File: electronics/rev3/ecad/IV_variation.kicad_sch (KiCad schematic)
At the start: 35 parts, among them Q5 TIP122, Q6 TIP127, U2 LMC6484A

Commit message: REV3 schematic
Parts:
- removed HS1, HS2: 15.60°C/W, symbol Mechanical:Heatsink
- removed Q5: TIP122, Package_TO_SOT_THT:TO-220-3_Vertical, symbol Transistor_BJT:TIP122
- removed Q6: TIP127, Package_TO_SOT_THT:TO-220-3_Vertical, symbol Transistor_BJT:TIP127
- removed R6, R7: 10k, Resistor_THT:R_Axial_DIN0207_L6.3mm_D2.5mm_P7.62mm_Horizontal, symbol Device:R_US
- removed R?: 1k, Resistor_THT:R_Axial_DIN0207_L6.3mm_D2.5mm_P7.62mm_Horizontal, symbol Device:R_US
- removed TP6: TestPoint, TestPoint:TestPoint_THTPad_D2.5mm_Drill1.2mm, symbol Connector:TestPoint
- removed unit 1 of U2
- added C10: 0.1uF, Capacitor_THT:C_Disc_D6.0mm_W2.5mm_P5.00mm, symbol Device:C
- added J1: DUT Connector, TerminalBlock_Phoenix:TerminalBlock_Phoenix_MKDS-1,5-2-5.08_1x02_P5.08mm_Horizontal, symbol Connector:Screw_Terminal_01x02
- added R36: 1.5, Resistor_THT:R_Axial_DIN0207_L6.3mm_D2.5mm_P7.62mm_Horizontal, symbol Device:R_US
- C7, C8: footprint (none) -> Capacitor_THT:C_Disc_D6.0mm_W2.5mm_P5.00mm; Distributor Part # (none) -> BC2662CT-ND; Part # (none) -> K103K10X7RF5UH5; Unit Price (none) -> 0.22
- D2: Distributor Part # (none) -> SA13CACT-ND; Part # (none) -> SA13CA; Unit Price (none) -> 0.49
- D3, D4, D5: Distributor Part # (none) -> 1727-2115-1-ND; Part # (none) -> BZX79-C2V4,113; Unit Price (none) -> 0.16
- F?: value 1A -> 1.5A; Distributor Part # (none) -> 507-1893-1-ND; Part # (none) -> 0685T1500-01; Unit Price (none) -> 0.32
- R10, R19: Distributor Part # (none) -> 1712-YR1B11K8CCCT-ND; Part # (none) -> YR1B11K8CC; Unit Price (none) -> 0.63
- R14, R15, R16, R17: Distributor Part # (none) -> A105970CT-ND; Part # (none) -> YR1B10KCC; Unit Price (none) -> 0.63
- R18, R20, R28, R8: Distributor Part # (none) -> A105942CT-ND; Part # (none) -> YR1B1K0CC; Unit Price (none) -> 0.63
- R23, R5: Distributor Part # (none) -> 1712-YR1B3K83CCCT-ND; Part # (none) -> YR1B3K83CC; Unit Price (none) -> 0.63
- R29: value 4.7k -> 3.83k+/-0.1%
- R30: Distributor Part # (none) -> 13-MFR-25FRF52-1KCT-ND; Part # (none) -> MFR-25FRF52-1K; Unit Price (none) -> 0.1
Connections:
- net GND: now also C10.2
- net Vmiddle: now also C10.1
- net V/2: now also R18.1, R29.1, R?.2
- net DUT+: no longer names the net of D2.2 (A2), R16.1, TP1.1
- net DUT+: now also J1.2 (Pin_2), R36.2
- net DUT-: no longer names the net of D2.1 (A1), F?.1, R15.1, TP5.1
- net DUT-: now also J1.1 (Pin_1)
- new net Sweep Voltage Buffer/Sweep_Amplified: R36.1
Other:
- added sheet Sweep Voltage Buffer (sweep_voltage_buffer.kicad_sch)
- sheet Half Supply Buffer ports: added V/2; removed none
- note added: "1.5W"
- note added: "4W"
- moved on the sheet: C7, C8, D2, D3, D4, D5, F?, R10, R14, R15, R16, R17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

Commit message: Layout work
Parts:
- added R?: 1+/-1%, Resistor_SMD:R_2512_6332Metric_Pad1.40x3.35mm_HandSolder, symbol Device:R_US
- F?: value 1.5A -> 1A
- R29: Distributor Part # (none) -> 1712-YR1B3K83CCCT-ND; Part # (none) -> YR1B3K83CC; Unit Price (none) -> 0.63
- R36: footprint Resistor_THT:R_Axial_DIN0207_L6.3mm_D2.5mm_P7.62mm_Horizontal -> Resistor_SMD:R_2512_6332Metric_Pad1.40x3.35mm_HandSolder; Distributor Part # (none) -> A121179CT-ND; Part # (none) -> 35221R5JT; Unit Price (none) -> 1.22
- R?: value 0.5+/-0.1% -> 1+/-1%; footprint Resistor_THT:R_Axial_DIN0207_L6.3mm_D2.5mm_P7.62mm_Horizontal -> Resistor_SMD:R_2512_6332Metric_Pad1.40x3.35mm_HandSolder; Distributor Part # (none) -> RMCF2512FT1R00CT-ND; Part # (none) -> RMCF2512FT1R00; Unit Price (none) -> 0.27
- TP1, TP3, TP4: Distributor Part # (none) -> 36-4952-ND; Part # (none) -> 4952; Unit Price (none) -> 0.26
- TP5: value TestPoint -> 4952; Distributor Part # (none) -> 36-4952-ND; Part # (none) -> 4952; Unit Price (none) -> 0.26
- U2: Distributor Part # (none) -> LMC6484IN/NOPB-ND; Part # (none) -> LMC6484IN/NOPB; Unit Price (none) -> 2.83
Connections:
- net V/2: now also R?.2
- net at F?.2, R8.1, R?.1: now also R?.1
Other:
- note added: "1W"
- note removed: "1.5W"
- moved on the sheet: C10, C7, C8, D2, D3, D4, D5, F?, J1, R10, R14, R15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

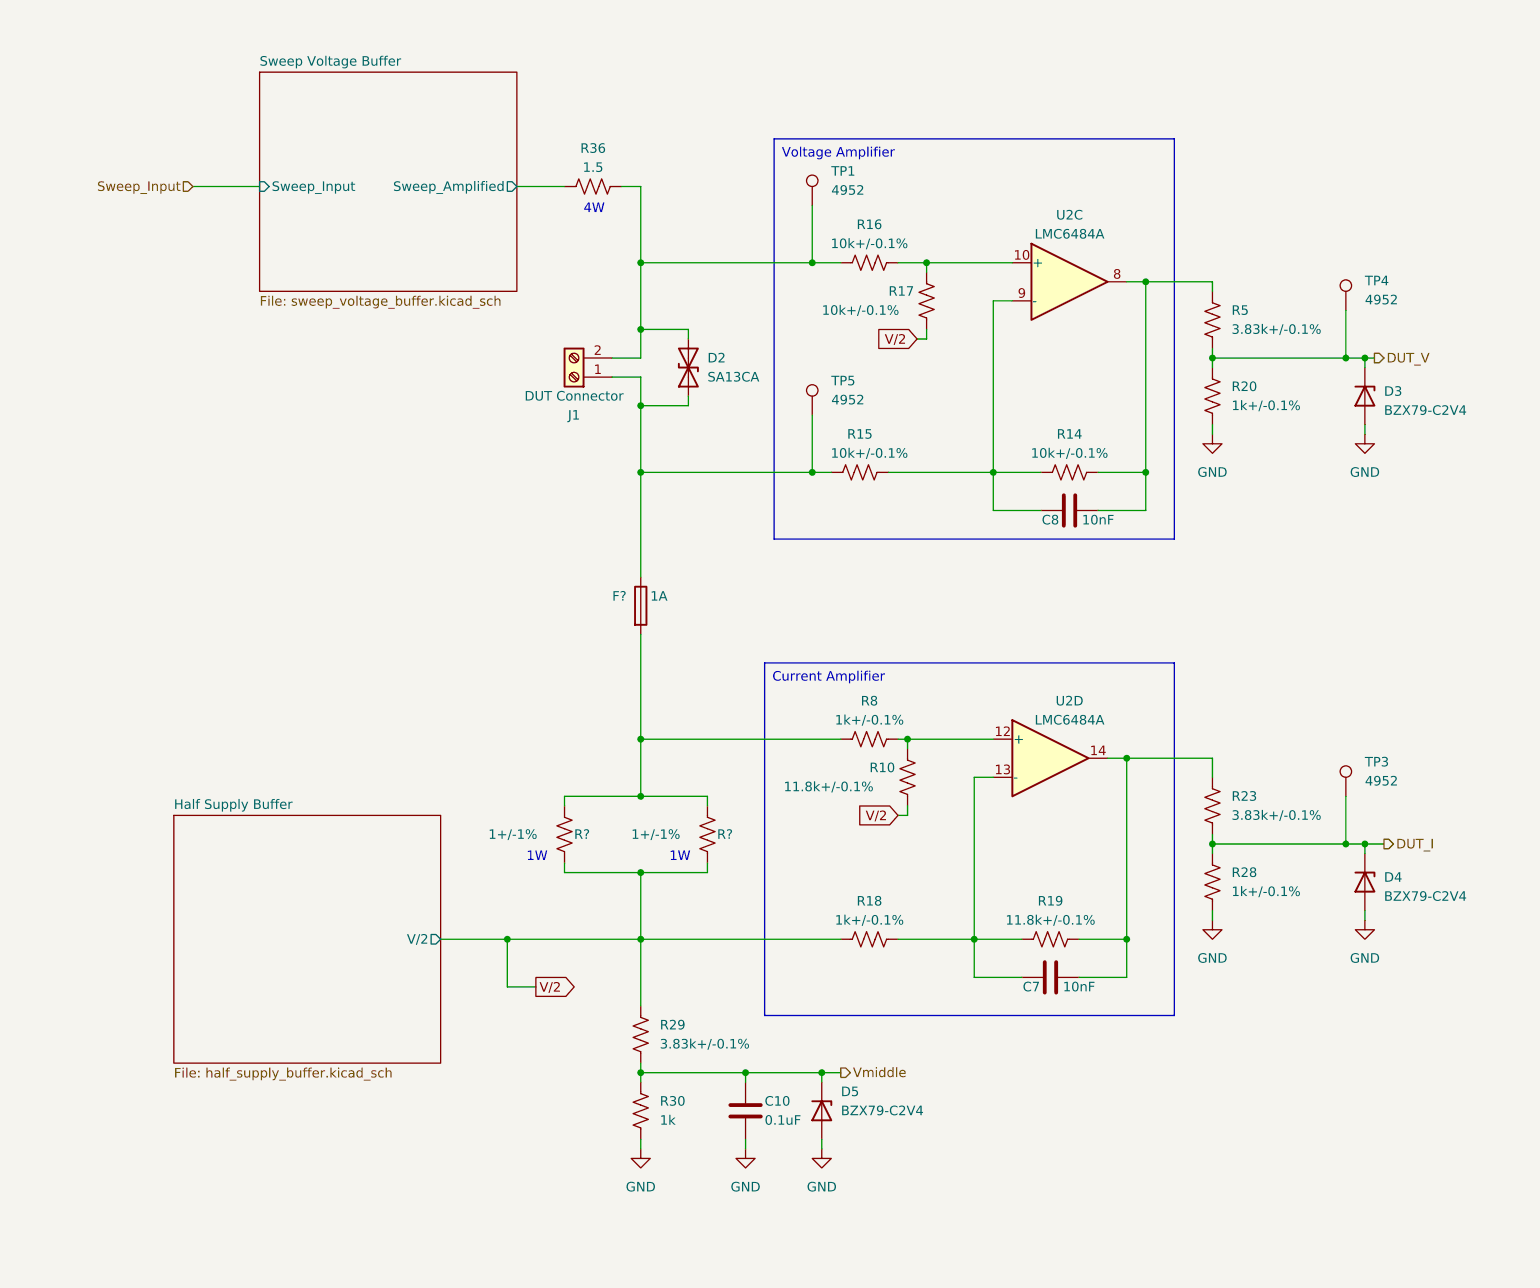
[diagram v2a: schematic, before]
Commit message: start direction modes
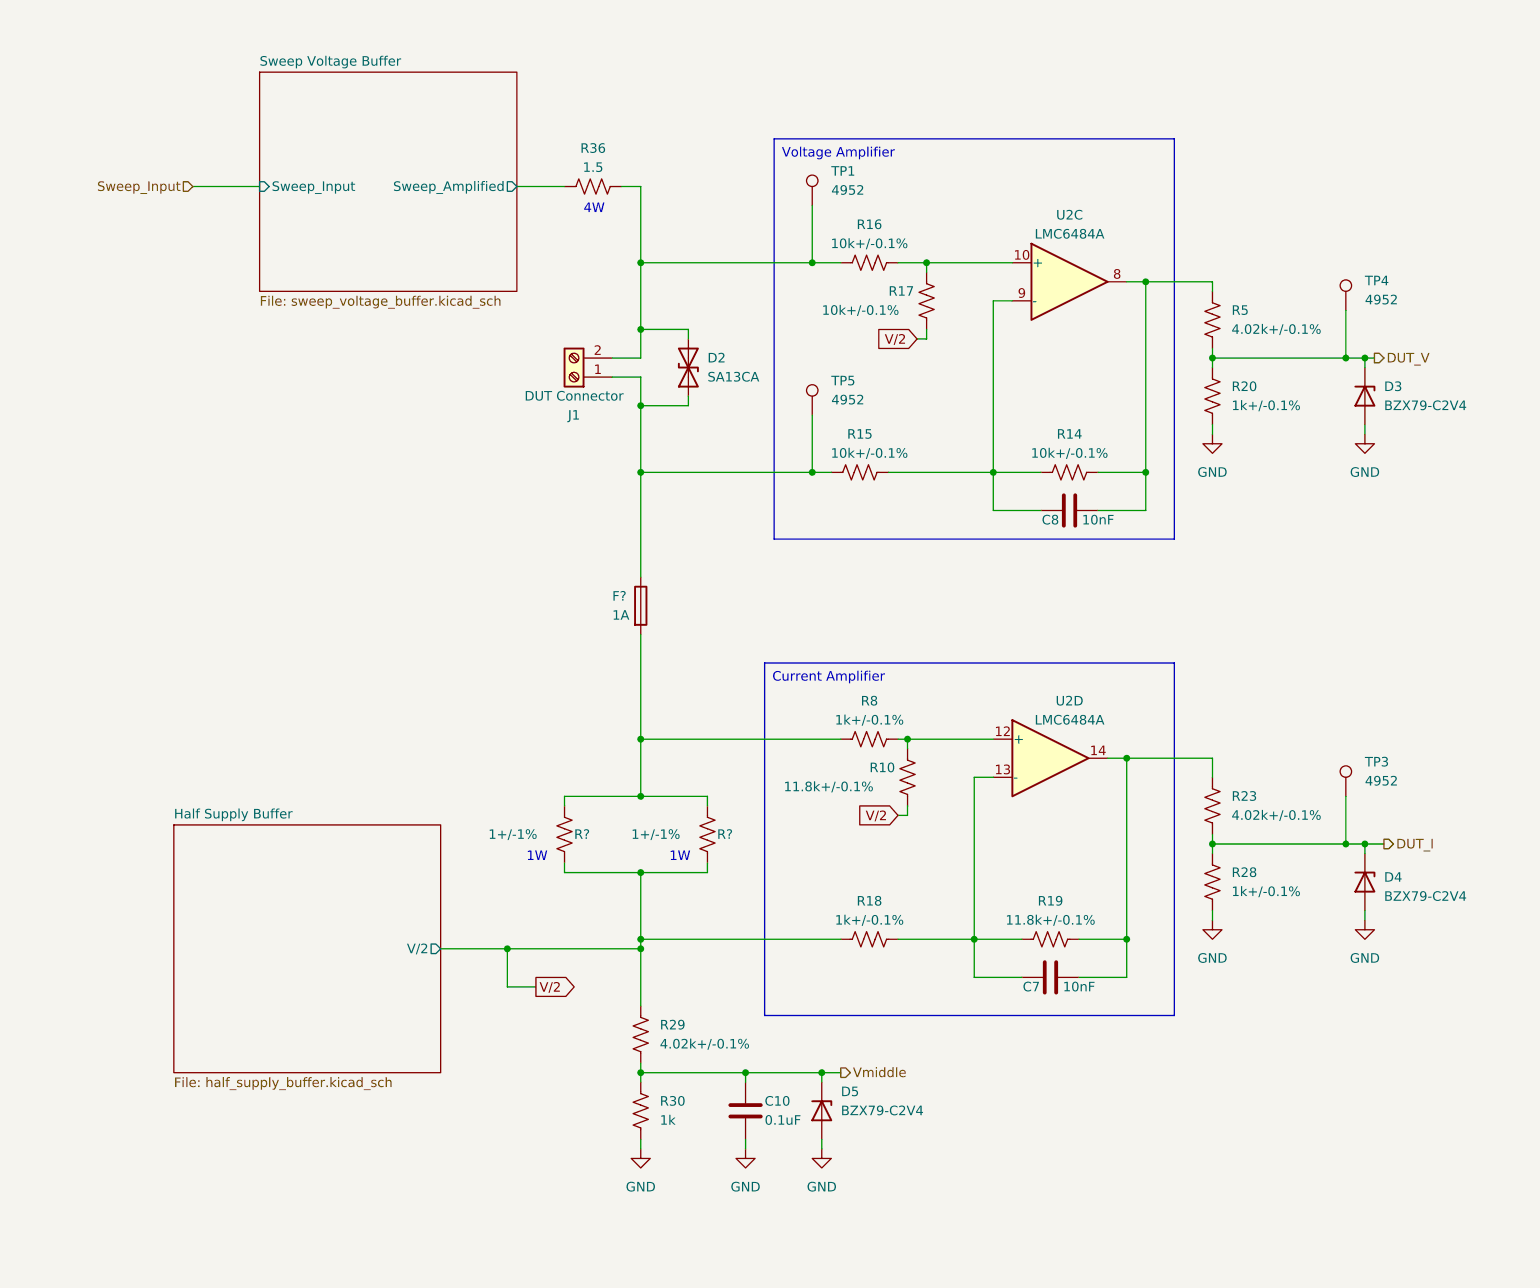
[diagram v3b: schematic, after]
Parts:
- R23, R29, R5: value 3.83k+/-0.1% -> 4.02k+/-0.1%
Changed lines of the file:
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@@
   (title_block
     (title "Analog Front End")
-    (date "2023-09-27")
+    (date "2023-10-10")
     (rev "3")
     (comment 1 "Designed by Marek Newton")
@@
   (junction (at 120.65 139.7) (diameter 0) (color 0 0 0 0)
   )
-  (junction (at 102.87 139.7) (diameter 0) (color 0 0 0 0)
-  )
   (junction (at 144.78 157.48) (diameter 0) (color 0 0 0 0)
   )
+  (junction (at 120.65 140.97) (diameter 0) (color 0 0 0 0)
+  )
   (junction (at 120.65 49.53) (diameter 0) (color 0 0 0 0)
   )
@@
   (junction (at 214.63 62.23) (diameter 0) (color 0 0 0 0)
   )
+  (junction (at 102.87 140.97) (diameter 0) (color 0 0 0 0)
+  )
   (junction (at 217.17 127) (diameter 0) (color 0 0 0 0)
   )
@@
     (stroke (width 0) (type default))
   )
-  (wire (pts (xy 102.87 139.7) (xy 102.87 146.05))
+  (wire (pts (xy 102.87 140.97) (xy 102.87 146.05))
     (stroke (width 0) (type default))
   )
@@
     (stroke (width 0) (type default))
   )
-  (wire (pts (xy 93.98 139.7) (xy 102.87 139.7))
+  (wire (pts (xy 93.98 140.97) (xy 102.87 140.97))
     (stroke (width 0) (type default))
   )
@@
     (stroke (width 0) (type default))
   )
-  (wire (pts (xy 120.65 139.7) (xy 120.65 148.59))
+  (wire (pts (xy 120.65 139.7) (xy 120.65 140.97))
     (stroke (width 0) (type default))
   )
@@
     (stroke (width 0) (type default))
   )
-  (wire (pts (xy 102.87 139.7) (xy 120.65 139.7))
-    (stroke (width 0) (type default))
-  )
   (wire (pts (xy 120.65 49.53) (xy 143.51 49.53))
     (stroke (width 0) (type default))
@@
     (stroke (width 0) (type default))
   )
+  (wire (pts (xy 102.87 140.97) (xy 120.65 140.97))
+    (stroke (width 0) (type default))
+  )
   (wire (pts (xy 165.1 144.78) (xy 171.45 144.78))
     (stroke (width 0) (type default))
@@
   )
   (wire (pts (xy 167.64 77.47) (xy 173.99 77.47))
+    (stroke (width 0) (type default))
+  )
+  (wire (pts (xy 120.65 140.97) (xy 120.65 148.59))
     (stroke (width 0) (type default))
   )
@@
       (effects (font (size 1.27 1.27)) (justify left))
     )
-    (property "Value" "3.83k+/-0.1%" (at 123.19 153.67 0)
+    (property "Value" "4.02k+/-0.1%" (at 123.19 153.67 0)
       (effects (font (size 1.27 1.27)) (justify left))
     )
@@
       (effects (font (size 1.27 1.27)) (justify left))
     )
-    (property "Value" "1A" (at 121.92 93.98 0)
+    (property "Value" "1A" (at 116.84 96.52 0)
       (effects (font (size 1.27 1.27)) (justify left))
     )
@@
       (effects (font (size 1.27 1.27)) (justify left))
     )
-    (property "Value" "3.83k+/-0.1%" (at 199.39 123.19 0)
+    (property "Value" "4.02k+/-0.1%" (at 199.39 123.19 0)
       (effects (font (size 1.27 1.27)) (justify left))
     )
@@
   (symbol (lib_id "Device:D_Zener") (at 217.17 67.31 270) (unit 1)
     (in_bom yes) (on_board yes) (dnp no) (fields_autoplaced)
-    (property "Reference" "D3" (at 219.71 66.675 90)
-      (effects (font (size 1.27 1.27)) (justify left))
-    )
-    (property "Value" "BZX79-C2V4" (at 219.71 69.215 90)
+    (property "Reference" "D3" (at 219.71 66.04 90)
+      (effects (font (size 1.27 1.27)) (justify left))
+    )
+    (property "Value" "BZX79-C2V4" (at 219.71 68.58 90)
       (effects (font (size 1.27 1.27)) (justify left))
     )
@@
       (effects (font (size 1.27 1.27)) (justify left))
     )
-    (property "Value" "3.83k+/-0.1%" (at 199.39 58.42 0)
+    (property "Value" "4.02k+/-0.1%" (at 199.39 58.42 0)
       (effects (font (size 1.27 1.27)) (justify left))
     )
@@
     )
   )
-  (sheet (at 58.42 123.19) (size 35.56 33.02) (fields_autoplaced)
+  (sheet (at 58.42 124.46) (size 35.56 33.02) (fields_autoplaced)
     (stroke (width 0.1524) (type solid))
     (fill (color 0 0 0 0.0000))
-    (property "Sheetname" "Half Supply Buffer" (at 58.42 122.4784 0)
+    (property "Sheetname" "Half Supply Buffer" (at 58.42 123.7484 0)
       (effects (font (size 1.27 1.27)) (justify left bottom))
     )
-    (property "Sheetfile" "half_supply_buffer.kicad_sch" (at 58.42 156.7946 0)
+    (property "Sheetfile" "half_supply_buffer.kicad_sch" (at 58.42 158.0646 0)
       (effects (font (size 1.27 1.27)) (justify left top))
     )
-    (pin "V{slash}2" output (at 93.98 139.7 0)
+    (pin "V{slash}2" output (at 93.98 140.97 0)
       (effects (font (size 1.27 1.27)) (justify right))
     )
